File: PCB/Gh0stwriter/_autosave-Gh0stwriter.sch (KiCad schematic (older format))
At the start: 20 parts, among them J1 Conn_01x06, J2 Conn_01x02, J3 Conn_01x06, J4 Conn_01x02, J5 Conn_01x06, J6 Conn_01x06, J7 Conn_01x02, Q1 Q_NPN_Darlington_ECB

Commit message: Most of pcb finished
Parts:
- C1, C2: footprint Capacitor_THT:CP_Radial_D8.0mm_P2.50mm -> Capacitor_THT:CP_Radial_D6.3mm_P2.50mm
- D1: footprint Diode_THT:D_DO-41_SOD81_P10.16mm_Horizontal -> Diode_THT:D_DO-35_SOD27_P2.54mm_Vertical_AnodeUp
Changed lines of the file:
@@
 F 0 "D1" H 5900 6217 50  0000 C CNN
 F 1 "1N4007" H 5900 6126 50  0000 C CNN
-F 2 "Diode_THT:D_DO-41_SOD81_P10.16mm_Horizontal" H 5900 5825 50  0001 C CNN
+F 2 "Diode_THT:D_DO-35_SOD27_P2.54mm_Vertical_AnodeUp" H 5900 5825 50  0001 C CNN
 F 3 "http://www.vishay.com/docs/88503/1n4001.pdf" H 5900 6000 50  0001 C CNN
 	1    5900 6000
@@
 F 0 "C2" H 2868 2596 50  0000 L CNN
 F 1 "CP" H 2868 2505 50  0000 L CNN
-F 2 "Capacitor_THT:CP_Radial_D8.0mm_P2.50mm" H 2788 2400 50  0001 C CNN
+F 2 "Capacitor_THT:CP_Radial_D6.3mm_P2.50mm" H 2788 2400 50  0001 C CNN
 F 3 "~" H 2750 2550 50  0001 C CNN
 	1    2750 2550
@@
 F 0 "C1" H 2518 2596 50  0000 L CNN
 F 1 "CP" H 2518 2505 50  0000 L CNN
-F 2 "Capacitor_THT:CP_Radial_D8.0mm_P2.50mm" H 2438 2400 50  0001 C CNN
+F 2 "Capacitor_THT:CP_Radial_D6.3mm_P2.50mm" H 2438 2400 50  0001 C CNN
 F 3 "~" H 2400 2550 50  0001 C CNN
 	1    2400 2550

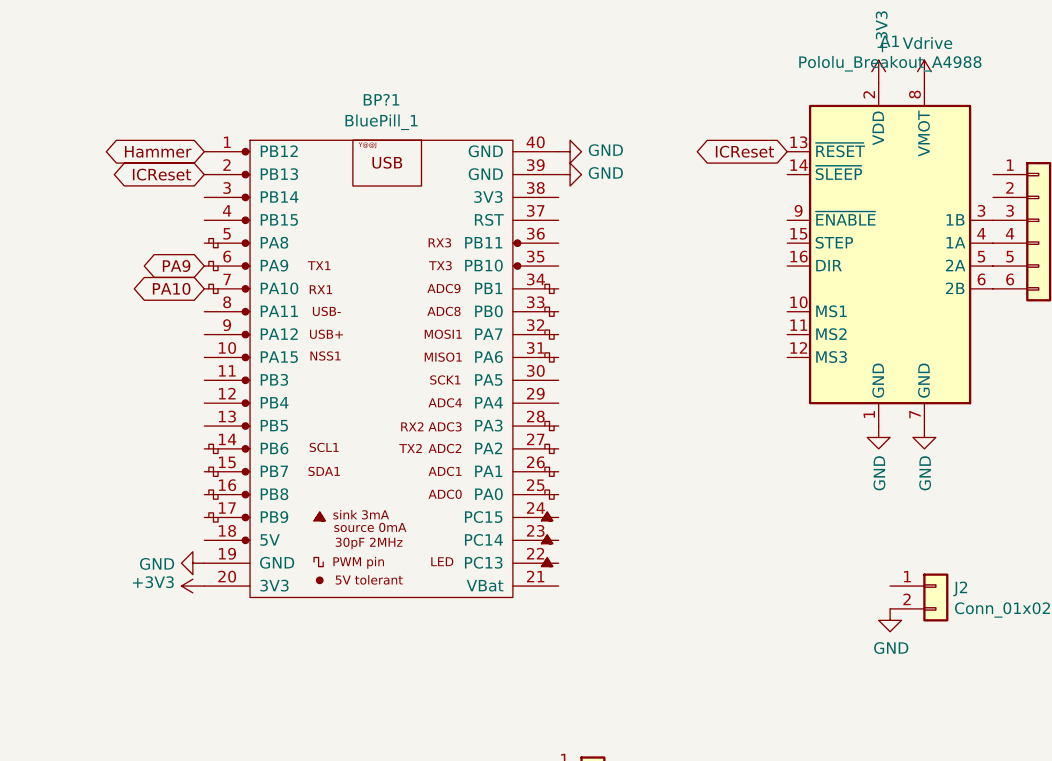
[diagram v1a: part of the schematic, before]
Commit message: Fixed clipping of parts
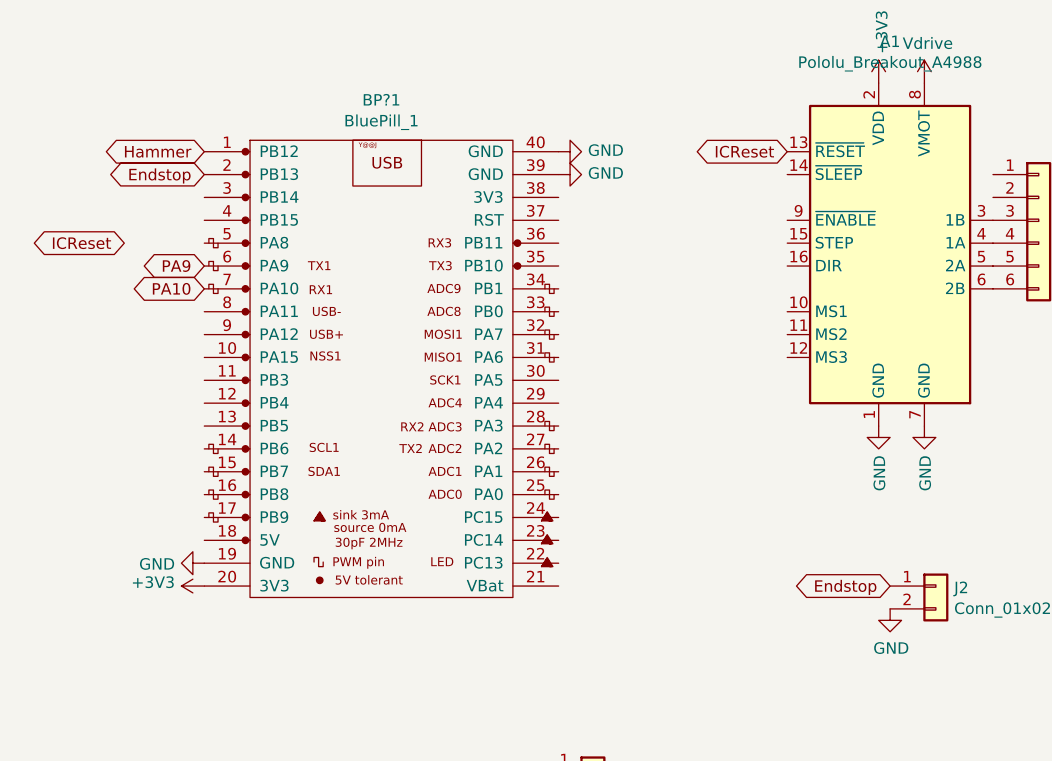
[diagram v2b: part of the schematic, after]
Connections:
- net ICReset: no longer BP?1.2 (PB13)
- net Endstop: now reaches J2.1 (Pin_1)
- net Endstop: now also BP?1.2 (PB13)
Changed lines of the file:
@@
 Text GLabel 9000 3850 0    50   BiDi ~ 0
 ICReset
-Text GLabel 1150 3900 0    50   BiDi ~ 0
+Text GLabel 800  4200 0    50   BiDi ~ 0
 ICReset
 $Comp
@@
 Text GLabel 5500 6350 0    50   BiDi ~ 0
 Hammer
+Text GLabel 4150 5700 0    50   BiDi ~ 0
+Endstop
+Text GLabel 1150 3900 0    50   BiDi ~ 0
+Endstop
 $EndSCHEMATC

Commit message: Finished first Version of the pcb
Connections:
- net ICReset: now also BP?1.12 (PB4); no longer A3.13 (~RESET)
- net A3STP: now reaches A3.15 (STEP)
- net A3STP: now also BP?1.14 (PB6)
- net A3DIR: now reaches A3.16 (DIR)
- net A3DIR: now also BP?1.13 (PB5)
- net A4DIR: now reaches BP?1.10 (PA15)
- net A4DIR: now also A4.16 (DIR)
- net A4STP: now reaches BP?1.11 (PB3)
- net A4STP: now also A4.15 (STEP)
- net A2DIR: now reaches BP?1.15 (PB7)
- net A2DIR: now also A2.16 (DIR)
- net A2STP: now reaches BP?1.16 (PB8)
- net A2STP: now also A2.15 (STEP)
- net A1STP: now reaches A1.15 (STEP)
- net A1DIR: now reaches A1.16 (DIR)
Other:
- moved on the sheet: A2, J3
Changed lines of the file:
@@
 L Driver_Motor:Pololu_Breakout_A4988 A2
 U 1 1 5ECFA6AE
-P 6250 4250
-F 0 "A2" H 6300 5131 50  0000 C CNN
-F 1 "Pololu_Breakout_A4988" H 6300 5040 50  0000 C CNN
-F 2 "Module:Pololu_Breakout-16_15.2x20.3mm" H 6525 3500 50  0001 L CNN
-F 3 "https://www.pololu.com/product/2980/pictures" H 6350 3950 50  0001 C CNN
-	1    6250 4250
+P 5900 3300
+F 0 "A2" H 5950 4181 50  0000 C CNN
+F 1 "Pololu_Breakout_A4988" H 5950 4090 50  0000 C CNN
+F 2 "Module:Pololu_Breakout-16_15.2x20.3mm" H 6175 2550 50  0001 L CNN
+F 3 "https://www.pololu.com/product/2980/pictures" H 6000 3000 50  0001 C CNN
+	1    5900 3300
 	1    0    0    -1
 $EndComp
@@
 L power:GND #PWR0111
 U 1 1 5ED7A1C8
-P 6250 5050
-F 0 "#PWR0111" H 6250 4800 50  0001 C CNN
-F 1 "GND" V 6255 4922 50  0000 R CNN
-F 2 "" H 6250 5050 50  0001 C CNN
-F 3 "" H 6250 5050 50  0001 C CNN
-	1    6250 5050
+P 5900 4100
+F 0 "#PWR0111" H 5900 3850 50  0001 C CNN
+F 1 "GND" V 5905 3972 50  0000 R CNN
+F 2 "" H 5900 4100 50  0001 C CNN
+F 3 "" H 5900 4100 50  0001 C CNN
+	1    5900 4100
 	1    0    0    -1
 $EndComp
@@
 L power:GND #PWR0112
 U 1 1 5ED7A4BD
-P 6450 5050
-F 0 "#PWR0112" H 6450 4800 50  0001 C CNN
-F 1 "GND" V 6455 4922 50  0000 R CNN
-F 2 "" H 6450 5050 50  0001 C CNN
-F 3 "" H 6450 5050 50  0001 C CNN
-	1    6450 5050
+P 6100 4100
+F 0 "#PWR0112" H 6100 3850 50  0001 C CNN
+F 1 "GND" V 6105 3972 50  0000 R CNN
+F 2 "" H 6100 4100 50  0001 C CNN
+F 3 "" H 6100 4100 50  0001 C CNN
+	1    6100 4100
 	1    0    0    -1
 $EndComp
@@
 L power:+3V3 #PWR0118
 U 1 1 5ED85A0B
-P 6250 3550
-F 0 "#PWR0118" H 6250 3400 50  0001 C CNN
-F 1 "+3V3" V 6265 3678 50  0000 L CNN
-F 2 "" H 6250 3550 50  0001 C CNN
-F 3 "" H 6250 3550 50  0001 C CNN
-	1    6250 3550
+P 5900 2600
+F 0 "#PWR0118" H 5900 2450 50  0001 C CNN
+F 1 "+3V3" V 5915 2728 50  0000 L CNN
+F 2 "" H 5900 2600 50  0001 C CNN
+F 3 "" H 5900 2600 50  0001 C CNN
+	1    5900 2600
 	1    0    0    -1
 $EndComp
@@
 L power:Vdrive #PWR0124
 U 1 1 5EDBB3D5
-P 6450 3550
-F 0 "#PWR0124" H 6250 3400 50  0001 C CNN
-F 1 "Vdrive" H 6465 3723 50  0000 C CNN
-F 2 "" H 6450 3550 50  0001 C CNN
-F 3 "" H 6450 3550 50  0001 C CNN
-	1    6450 3550
+P 6100 2600
+F 0 "#PWR0124" H 5900 2450 50  0001 C CNN
+F 1 "Vdrive" H 6115 2773 50  0000 C CNN
+F 2 "" H 6100 2600 50  0001 C CNN
+F 3 "" H 6100 2600 50  0001 C CNN
+	1    6100 2600
 	1    0    0    -1
 $EndComp
@@
 Text GLabel 3700 3800 0    50   BiDi ~ 0
 ICReset
-Text GLabel 5850 3850 0    50   BiDi ~ 0
+Text GLabel 5500 2900 0    50   BiDi ~ 0
 ICReset
-Text GLabel 7200 3850 0    50   BiDi ~ 0
+Text GLabel 6850 2900 0    50   BiDi ~ 0
 ICReset
 Text GLabel 9000 3850 0    50   BiDi ~ 0
 ICReset
-Text GLabel 800  4200 0    50   BiDi ~ 0
+Text GLabel 1150 4900 0    50   BiDi ~ 0
 ICReset
 $Comp
 L Connector_Generic:Conn_01x06 J3
 U 1 1 5EE5F861
-P 6950 4150
-F 0 "J3" H 7030 4142 50  0000 L CNN
-F 1 "Conn_01x06" H 7030 4051 50  0000 L CNN
-F 2 "Connector_JST:JST_XH_B6B-XH-A_1x06_P2.50mm_Vertical" H 6950 4150 50  0001 C CNN
-F 3 "~" H 6950 4150 50  0001 C CNN
-	1    6950 4150
+P 6600 3200
+F 0 "J3" H 6680 3192 50  0000 L CNN
+F 1 "Conn_01x06" H 6680 3101 50  0000 L CNN
+F 2 "Connector_JST:JST_XH_B6B-XH-A_1x06_P2.50mm_Vertical" H 6600 3200 50  0001 C CNN
+F 3 "~" H 6600 3200 50  0001 C CNN
+	1    6600 3200
 	1    0    0    -1
 $EndComp
@@
 Text GLabel 1150 3900 0    50   BiDi ~ 0
 Endstop
+Text GLabel 1150 4700 0    50   BiDi ~ 0
+A4DIR
+Text GLabel 1150 4800 0    50   BiDi ~ 0
+A4STP
+Text GLabel 9000 4250 0    50   BiDi ~ 0
+A4STP
+Text GLabel 9000 4350 0    50   BiDi ~ 0
+A4DIR
+Text GLabel 7200 4250 0    50   BiDi ~ 0
+A3STP
+Text GLabel 7200 4350 0    50   BiDi ~ 0
+A3DIR
+Text GLabel 5500 3300 0    50   BiDi ~ 0
+A2STP
+Text GLabel 5500 3400 0    50   BiDi ~ 0
+A2DIR
+Text GLabel 3700 4200 0    50   BiDi ~ 0
+A1STP
+Text GLabel 3700 4300 0    50   BiDi ~ 0
+A1DIR
+Text GLabel 1150 5000 0    50   BiDi ~ 0
+A3DIR
+Text GLabel 1150 5100 0    50   BiDi ~ 0
+A3STP
+Text GLabel 1150 5200 0    50   BiDi ~ 0
+A2DIR
+Text GLabel 1150 5300 0    50   BiDi ~ 0
+A2STP
 $EndSCHEMATC
